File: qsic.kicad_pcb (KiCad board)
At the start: 6 copper layers, 214.1 x 131.7 mm, 217 parts, among them J201 USB_microB, J202 DM3BT-DSF-PEJS, J203 USB_A, J204 DM3BT-DSF-PEJS, J401 QBUS_A, J402 QBUS_B, P201 02x05 Right Angle Shrouded, U101 MT25Q, U102 XC7A75T-1CSG324, U201 FT2232HQ, U202 93LC46C-I/MC, U203 TPS2561, U204 MAX3033E, U205 USB3340, U301 TPS82085, U302 TPS82085, U303 TPS82085, U304 TPS82085, U401 DS8641-LR, U402 DS8641-LR, U403 74LVC8T245, U404 74LVC8T245, U405 74LVC8T245, U406 74LVC8T245, U407 DS8641-LR, U408 DS8641-LR, U409 DS8641-LR, U410 DS8641-LR, U411 74LVC8T245, U412 74LVC8T245, U413 74LVC8T245, U414 74LVC8T245, U415 DS8641-LR, U416 DS8641-LR, U417 74LVC8T245, U418 DS8641-LR, U419 DS8641-LR, U420 74LVC8T245, U421 74LVC8T245, U422 DS8641-LR, U501 MT41J128M16JT-125, U502 TPS51206, X201 ASE-24.000MHz, Y201 12 MHz

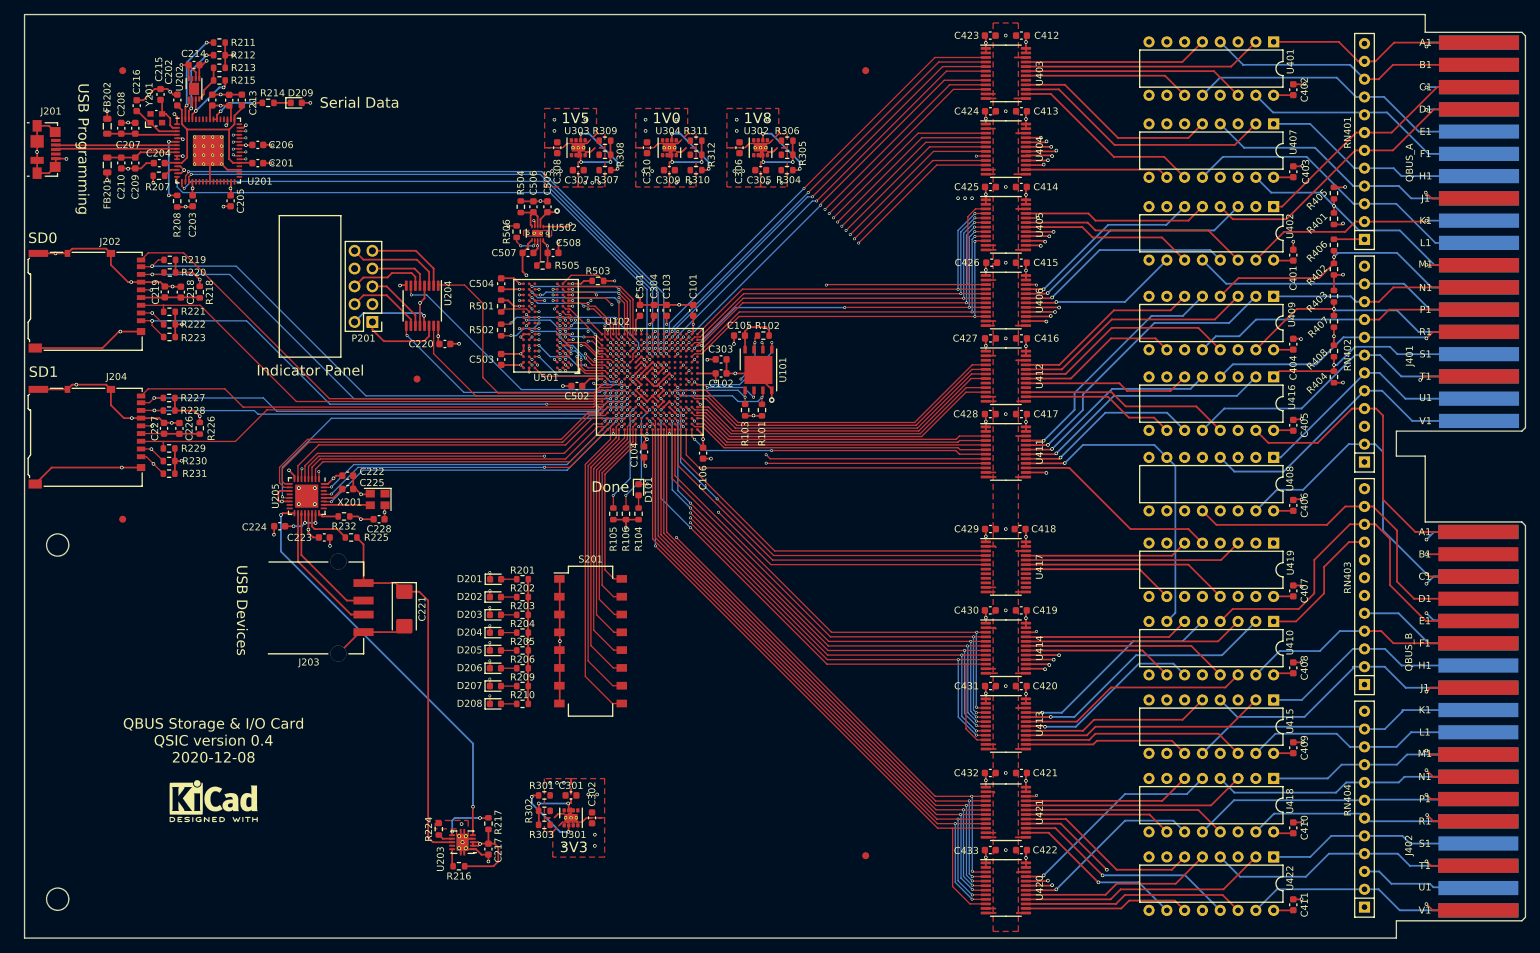
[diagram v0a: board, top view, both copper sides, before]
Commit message: Cleaned up the directory and renamed files.  Also converted from the 324 package on the FPGA to the 484 package.  That conversion is still in-progress.
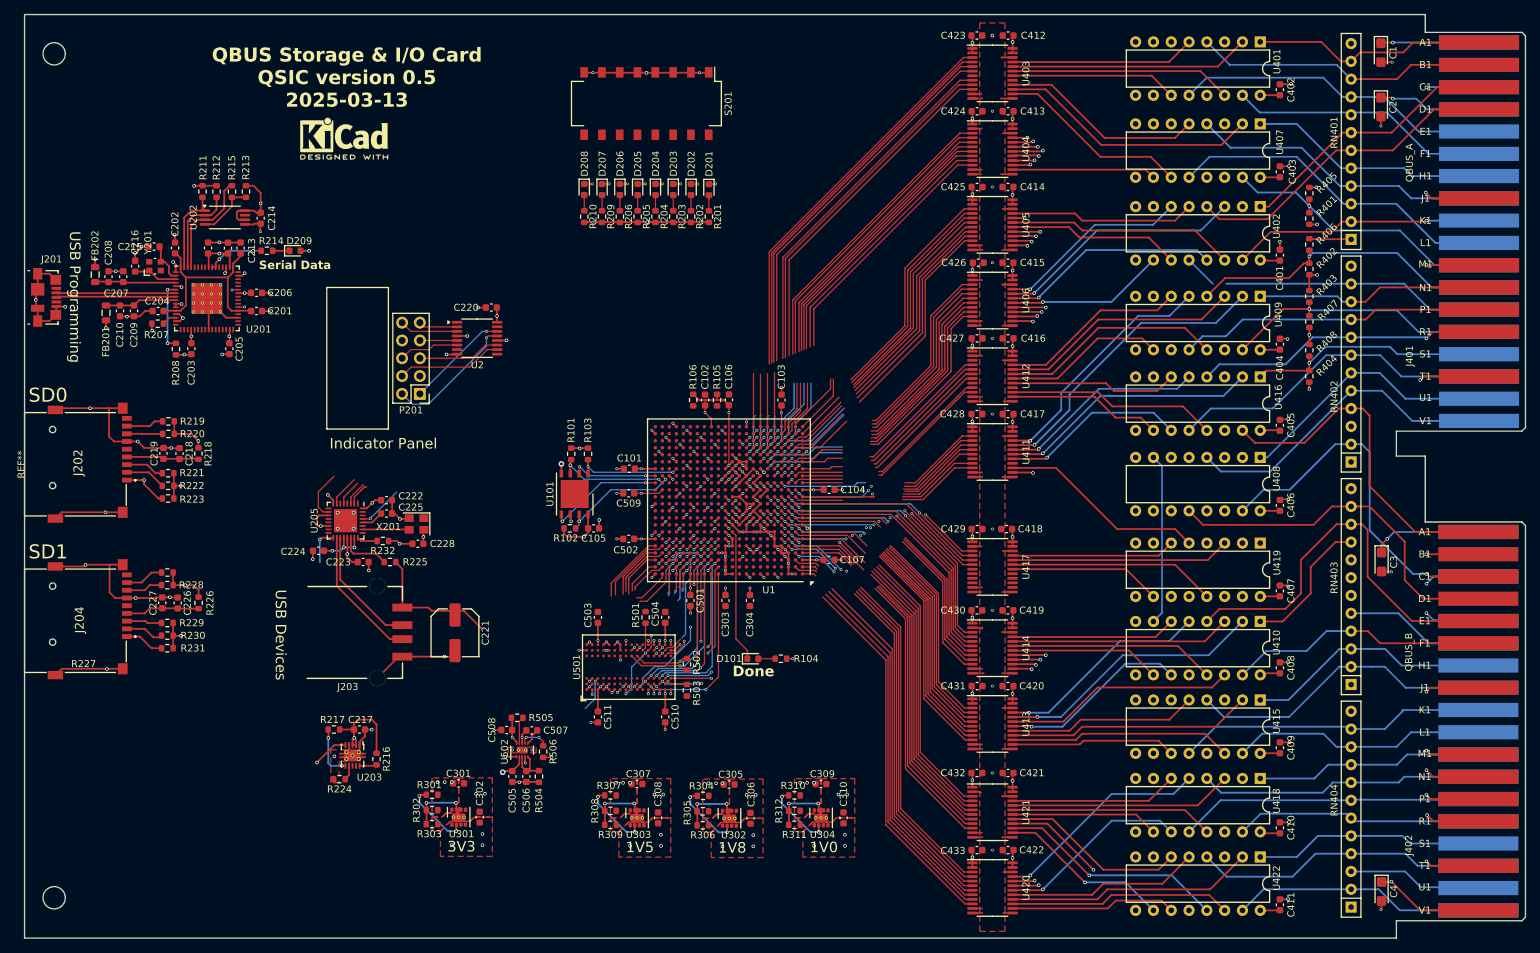
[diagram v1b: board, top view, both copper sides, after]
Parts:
- removed FID101, FID102, FID103, FID104, FID105: Fiducial, Fiducial:Fiducial_1mm_Mask2mm
- removed the REF** at (33.0, 126.3)
- removed U102: XC7A75T-1CSG324, Package_BGA:Xilinx_CSG324
- removed U204: MAX3033E, Package_SO:TSSOP-16_4.4x5mm_P0.65mm
- added C1: 10 uF 16V, Capacitor_Tantalum_SMD:CP_EIA-3216-18_Kemet-A, F.Cu at (226.5, 30.9)
- added C107: 22µF, Capacitor_SMD:C_0603_1608Metric, F.Cu at (147.8, 103.2)
- added C2: 10 uF 16V, Capacitor_Tantalum_SMD:CP_EIA-3216-18_Kemet-A, F.Cu at (226.5, 38.6)
- added C3: 10 uF 16V, Capacitor_Tantalum_SMD:CP_EIA-3216-18_Kemet-A, F.Cu at (226.6, 103.5)
- added C4: 10 uF 16V, Capacitor_Tantalum_SMD:CP_EIA-3216-18_Kemet-A, F.Cu at (226.6, 150.5)
- added C509: 22µF, Capacitor_SMD:C_0603_1608Metric, F.Cu at (119.2, 93.7)
- added C510: 10µF, Capacitor_SMD:C_0603_1608Metric, F.Cu at (124.4, 125.6)
- added C511: 10µF, Capacitor_SMD:C_0603_1608Metric, F.Cu at (114.8, 125.6)
- added REF**: Untitled, DEC:DEChandle QSIC, F.Cu at (33.1, 91.2)
- added U1: XC7A75T-2FGG484, Package_BGA:Xilinx_FGG484, F.Cu at (133.5, 94.7)
- added U2: AM26LV31EIPWR, Package_SO:TSSOP-16_4.4x5mm_P0.65mm, F.Cu at (97.6, 71.6)
- C101, C102, C103, C104, C106, C218, C226, C301, C305, C307, C309, C501, C502: value 22µF 10V -> 22µF
- C221: footprint Capacitor_Tantalum_SMD:CP_EIA-6032-28_Kemet-C -> Capacitor_SMD:C_Elec_6.3x7.7
- C503, C504: value 10µF 10V -> 10µF
- J202, J204: value DM3BT-DSF-PEJS -> TF-15x15; footprint Connector_Card:microSD_HC_Hirose_DM3AT-SF-PEJM5 -> Imports:TF15X15
- R104, R201, R202, R203, R204, R205, R206, R209, R210, R214: value 240 -> 330
- U202: value 93LC46C-I/MC -> 93LC46BT-I/ST; footprint Package_DFN_QFN:DFN-8-1EP_3x2mm_P0.5mm_EP1.75x1.45mm -> Package_SO:TSSOP-8_4.4x3mm_P0.65mm
- moved C310 99.6 mm to (149.9, 140.0), turned to 90 degrees
- moved R312 98.6 mm to (142.9, 141.0), turned to 0 degrees
- moved R306 98.4 mm to (129.8, 141.1), turned to 0 degrees
- moved U304 98.0 mm to (146.7, 140.0), turned to 90 degrees
- moved R309 97.6 mm to (116.6, 141.0), turned to 0 degrees
- moved C308 96.7 mm to (123.4, 140.0), turned to 90 degrees
- moved LOGO101 96.3 mm to (78.6, 43.1)
- moved U303 96.0 mm to (120.4, 140.0), turned to 90 degrees
- moved U302 95.8 mm to (133.6, 140.1), turned to 90 degrees
- moved C306 95.7 mm to (136.6, 140.1), turned to 90 degrees
- moved R311 94.6 mm to (142.9, 139.0), turned to 180 degrees
- moved R305 94.4 mm to (129.8, 139.1), turned to 180 degrees
- moved R308 93.6 mm to (116.6, 139.0), turned to 180 degrees
- moved R310 90.3 mm to (142.9, 136.8), turned to 180 degrees
- moved C309 90.2 mm to (146.6, 135.2), turned to 0 degrees
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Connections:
- net /I/O/D+ renamed /IO/D+
- net /I/O/D- renamed /IO/D-
- P201 pad 1: /I/O/IPdata_P -> /IO/IPdata_P
- P201 pad 10: /I/O/IPclk_N -> /IO/IPclk_N
- P201 pad 2: /I/O/IPdata_N -> /IO/IPdata_N
- P201 pad 4: /I/O/IPlatch_P -> /IO/IPlatch_P
- P201 pad 5: /I/O/IPlatch_N -> /IO/IPlatch_N
- P201 pad 6: /I/O/IPblank_P -> /IO/IPblank_P
- P201 pad 7: /I/O/IPblank_N -> /IO/IPblank_N
- P201 pad 9: /I/O/IPclk_P -> /IO/IPclk_P
- U402 pad 7: /QBUS/~{TxDAL_5} -> GND
- U405 pad 10: /ZDAL19 -> /TDAL19
- U405 pad 3: /ZDAL17 -> /TDAL17
- U405 pad 4: /ZDAL16 -> /TDAL16
- U405 pad 5: /ZWTBT -> /TWTBT
- U405 pad 6: /ZBS7 -> /TBS7
- U405 pad 7: /ZDAL1 -> /TDAL1
- U405 pad 8: /ZDAL0 -> /TDAL0
- U405 pad 9: /ZDAL18 -> /TDAL18
- U406 pad 10: /ZDAL19 -> /RDAL19
- U406 pad 22: /~{RxDAL} -> GND
- U406 pad 3: /ZDAL17 -> /RDAL17
- U406 pad 4: /ZDAL16 -> /RDAL16
- U406 pad 5: /ZWTBT -> /RWTBT
- U406 pad 6: /ZBS7 -> /RBS7
- U406 pad 7: /ZDAL1 -> /RDAL1
- U406 pad 8: /ZDAL0 -> /RDAL0
- U406 pad 9: /ZDAL18 -> /RDAL18
- U408 pad 7: /QBUS/~{TxDAL_5} -> GND
- U410 pad 7: /QBUS/~{TxDAL_5} -> GND
- U411 pad 16: /QBUS/~{TxDAL_5} -> unconnected-(U411-B5-Pad16)
- U411 pad 8: /~{TxDAL} -> unconnected-(U411-A5-Pad8)
- U413 pad 10: /ZDAL6 -> /TDAL6
- U413 pad 3: /ZDAL20 -> /TDAL20
- U413 pad 4: /ZDAL2 -> /TDAL2
- U413 pad 5: /ZDAL21 -> /TDAL21
- U413 pad 6: /ZDAL3 -> /TDAL3
- U413 pad 7: /ZDAL5 -> /TDAL5
- U413 pad 8: /ZDAL4 -> /TDAL4
- U413 pad 9: /ZDAL7 -> /TDAL7
- U414 pad 10: /ZDAL6 -> /RDAL6
- U414 pad 22: /~{RxDAL} -> GND
- U414 pad 3: /ZDAL20 -> /RDAL20
- U414 pad 4: /ZDAL2 -> /RDAL2
- U414 pad 5: /ZDAL21 -> /RDAL21
- U414 pad 6: /ZDAL3 -> /RDAL3
- U414 pad 7: /ZDAL5 -> /RDAL5
- U414 pad 8: /ZDAL4 -> /RDAL4
- U414 pad 9: /ZDAL7 -> /RDAL7
- U415 pad 7: /QBUS/~{TxDAL_5} -> GND
- U418 pad 7: /QBUS/~{TxDAL_5} -> GND
- U420 pad 10: /ZDAL14 -> /TDAL14
- U420 pad 3: /ZDAL9 -> /TDAL9
- U420 pad 4: /ZDAL8 -> /TDAL8
- U420 pad 5: /ZDAL11 -> /TDAL11
- U420 pad 6: /ZDAL10 -> /TDAL10
- U420 pad 7: /ZDAL13 -> /TDAL13
- U420 pad 8: /ZDAL12 -> /TDAL12
- U420 pad 9: /ZDAL15 -> /TDAL15
- U421 pad 10: /ZDAL14 -> /RDAL14
- U421 pad 22: /~{RxDAL} -> GND
- U421 pad 3: /ZDAL9 -> /RDAL9
- U421 pad 4: /ZDAL8 -> /RDAL8
- U421 pad 5: /ZDAL11 -> /RDAL11
- U421 pad 6: /ZDAL10 -> /RDAL10
- U421 pad 7: /ZDAL13 -> /RDAL13
- U421 pad 8: /ZDAL12 -> /RDAL12
- U421 pad 9: /ZDAL15 -> /RDAL15
- U422 pad 7: /QBUS/~{TxDAL_5} -> GND
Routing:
- net /~{RxDAL}: track 132.2 -> 0.00 mm, vias 4 -> 0
- net GND: track 440.5 -> 565.4 mm, vias 148 -> 191
- net /QBUS/~{TxDAL_5}: track 119.8 -> 0.00 mm, vias 1 -> 0
- net /ZDAL14: track 96.6 -> 0.00 mm, vias 2 -> 0
- net /ZDAL12: track 94.6 -> 0.00 mm, vias 2 -> 0
- net /ZDAL15: track 93.7 -> 0.00 mm, vias 2 -> 0
- net /ZDAL10: track 91.8 -> 0.00 mm, vias 2 -> 0
- net /ZDAL13: track 91.8 -> 0.00 mm, vias 2 -> 0
- net /ZDAL9: track 91.3 -> 0.00 mm, vias 4 -> 0
- net /ZDAL8: track 90.0 -> 0.00 mm, vias 2 -> 0
- net /ZDAL11: track 89.9 -> 0.00 mm, vias 2 -> 0
- net /TDO: track 86.0 -> 0.00 mm, vias 2 -> 0
- net /TDI: track 84.5 -> 0.00 mm, vias 2 -> 0
- net /TCK: track 84.4 -> 0.00 mm, vias 2 -> 0
- net /TMS: track 84.3 -> 0.00 mm, vias 2 -> 0
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- removed copper zone on In2.Cu, net /3V3
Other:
- board text added: "QBUS Storage & I/O Card QSIC version ${REVISION} ${ISSUE_DATE}"
- board text removed: "Done"
- board text removed: "QBUS Storage & I/O Card QSIC version 0.4 2020-12-08"

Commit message: Switched the level converters to 74HCT2G04 and 75LVC2G04.  Still need to remap the FPGA pins to the signal odering.
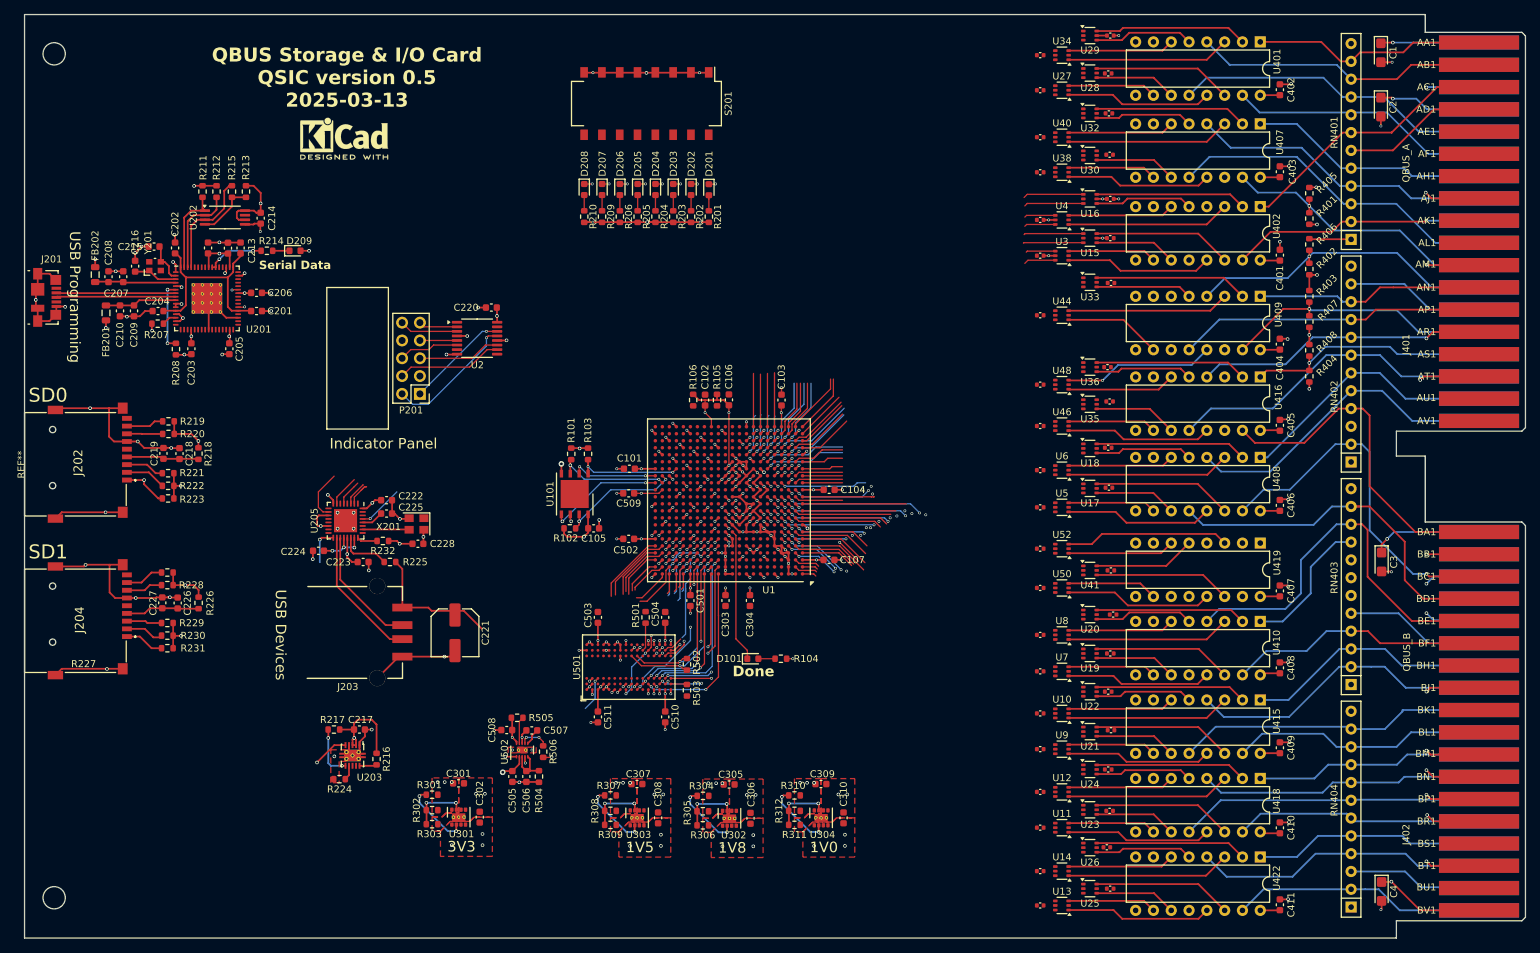
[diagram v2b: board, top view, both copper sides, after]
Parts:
- removed C412, C413, C414, C415, C416, C417, C418, C419, C420, C421, C422, C423, C424, C425, C426, C427, C428, C429, C430, C431, C432, C433: 100nF, Capacitor_SMD:C_0603_1608Metric
- removed U403, U404, U405, U406, U411, U412, U413, U414, U417, U420, U421: 74LVC8T245, Package_SO:TSSOP-24_4.4x7.8mm_P0.65mm
- added C464: 100nF, Capacitor_SMD:C_0402_1005Metric, F.Cu at (177.9, 54.7)
- added C465: 100nF, Capacitor_SMD:C_0402_1005Metric, F.Cu at (177.9, 59.8)
- added C466: 100nF, Capacitor_SMD:C_0402_1005Metric, F.Cu at (177.9, 84.1)
- added C467: 100nF, Capacitor_SMD:C_0402_1005Metric, F.Cu at (177.9, 68.3)
- added C469: 100nF, Capacitor_SMD:C_0402_1005Metric, F.Cu at (177.9, 78.2)
- added C470: 100nF, Capacitor_SMD:C_0402_1005Metric, F.Cu at (177.9, 47.9)
- added C471: 100nF, Capacitor_SMD:C_0402_1005Metric, F.Cu at (177.9, 42.9)
- added C472: 100nF, Capacitor_SMD:C_0402_1005Metric, F.Cu at (177.9, 31.2)
- added C473: 100nF, Capacitor_SMD:C_0402_1005Metric, F.Cu at (177.9, 36.2)
- added C474: 100nF, Capacitor_SMD:C_0402_1005Metric, F.Cu at (177.9, 101.6)
- added C475: 100nF, Capacitor_SMD:C_0402_1005Metric, F.Cu at (177.9, 95.7)
- added C476: 100nF, Capacitor_SMD:C_0402_1005Metric, F.Cu at (177.9, 90.4)
- added C477: 100nF, Capacitor_SMD:C_0402_1005Metric, F.Cu at (187.9, 57.3)
- added C478: 100nF, Capacitor_SMD:C_0402_1005Metric, F.Cu at (187.9, 51.7)
- added C479: 100nF, Capacitor_SMD:C_0402_1005Metric, F.Cu at (187.6, 133.1)
- added C480: 100nF, Capacitor_SMD:C_0402_1005Metric, F.Cu at (187.8, 139.0)
- added C481: 100nF, Capacitor_SMD:C_0402_1005Metric, F.Cu at (187.4, 144.2)
- added C482: 100nF, Capacitor_SMD:C_0402_1005Metric, F.Cu at (187.9, 150.1)
- added C483: 100nF, Capacitor_SMD:C_0402_1005Metric, F.Cu at (187.7, 39.5)
- added C484: 100nF, Capacitor_SMD:C_0402_1005Metric, F.Cu at (187.6, 87.2)
- added C485: 100nF, Capacitor_SMD:C_0402_1005Metric, F.Cu at (187.7, 92.9)
- added C486: 100nF, Capacitor_SMD:C_0402_1005Metric, F.Cu at (188.3, 111.0)
- added C487: 100nF, Capacitor_SMD:C_0402_1005Metric, F.Cu at (187.9, 116.5)
- added C488: 100nF, Capacitor_SMD:C_0402_1005Metric, F.Cu at (187.6, 122.0)
- added C489: 100nF, Capacitor_SMD:C_0402_1005Metric, F.Cu at (188.0, 127.5)
- added C490: 100nF, Capacitor_SMD:C_0402_1005Metric, F.Cu at (177.9, 107.2)
- added C491: 100nF, Capacitor_SMD:C_0402_1005Metric, F.Cu at (187.9, 28.4)
- added C492: 100nF, Capacitor_SMD:C_0402_1005Metric, F.Cu at (177.9, 152.5)
- added C493: 100nF, Capacitor_SMD:C_0402_1005Metric, F.Cu at (187.8, 45.4)
- added C494: 100nF, Capacitor_SMD:C_0402_1005Metric, F.Cu at (177.9, 141.4)
- added C495: 100nF, Capacitor_SMD:C_0402_1005Metric, F.Cu at (188.0, 104.7)
- added C496: 100nF, Capacitor_SMD:C_0402_1005Metric, F.Cu at (177.9, 130.2)
- added C499: 100nF, Capacitor_SMD:C_0402_1005Metric, F.Cu at (187.8, 80.6)
- added C500: 100nF, Capacitor_SMD:C_0402_1005Metric, F.Cu at (177.9, 113.9)
- added C512: 100nF, Capacitor_SMD:C_0402_1005Metric, F.Cu at (187.6, 33.8)
- added C513: 100nF, Capacitor_SMD:C_0402_1005Metric, F.Cu at (177.9, 147.6)
- added C514: 100nF, Capacitor_SMD:C_0402_1005Metric, F.Cu at (188.0, 63.7)
- added C515: 100nF, Capacitor_SMD:C_0402_1005Metric, F.Cu at (177.9, 136.3)
- added C516: 100nF, Capacitor_SMD:C_0402_1005Metric, F.Cu at (187.5, 75.7)
- added C517: 100nF, Capacitor_SMD:C_0402_1005Metric, F.Cu at (177.9, 125.1)
- added C519: 100nF, Capacitor_SMD:C_0402_1005Metric, F.Cu at (177.9, 119.1)
- added U10: 74LVC2GU04, Package_TO_SOT_SMD:SOT-363_SC-70-6, F.Cu at (181.0, 125.1)
- added U11: 74LVC2GU04, Package_TO_SOT_SMD:SOT-363_SC-70-6, F.Cu at (181.0, 141.4)
- added U12: 74LVC2GU04, Package_TO_SOT_SMD:SOT-363_SC-70-6, F.Cu at (181.0, 136.3)
- added U13: 74LVC2GU04, Package_TO_SOT_SMD:SOT-363_SC-70-6, F.Cu at (181.0, 152.5)
- added U14: 74LVC2GU04, Package_TO_SOT_SMD:SOT-363_SC-70-6, F.Cu at (181.0, 147.6)
- added U15: 74HCT2GU04, Package_TO_SOT_SMD:SOT-363_SC-70-6, F.Cu at (185.0, 57.3)
- added U16: 74HCT2GU04, Package_TO_SOT_SMD:SOT-363_SC-70-6, F.Cu at (185.0, 51.7)
- added U17: 74HCT2GU04, Package_TO_SOT_SMD:SOT-363_SC-70-6, F.Cu at (185.0, 93.0)
- added U18: 74HCT2GU04, Package_TO_SOT_SMD:SOT-363_SC-70-6, F.Cu at (185.0, 87.3)
- added U19: 74HCT2GU04, Package_TO_SOT_SMD:SOT-363_SC-70-6, F.Cu at (185.0, 116.5)
- added U20: 74HCT2GU04, Package_TO_SOT_SMD:SOT-363_SC-70-6, F.Cu at (185.0, 111.0)
- added U21: 74HCT2GU04, Package_TO_SOT_SMD:SOT-363_SC-70-6, F.Cu at (185.0, 127.7)
- added U22: 74HCT2GU04, Package_TO_SOT_SMD:SOT-363_SC-70-6, F.Cu at (185.0, 122.0)
- added U23: 74HCT2GU04, Package_TO_SOT_SMD:SOT-363_SC-70-6, F.Cu at (185.0, 138.8)
- added U24: 74HCT2GU04, Package_TO_SOT_SMD:SOT-363_SC-70-6, F.Cu at (185.0, 133.1)
- added U25: 74HCT2GU04, Package_TO_SOT_SMD:SOT-363_SC-70-6, F.Cu at (185.0, 150.1)
- added U26: 74HCT2GU04, Package_TO_SOT_SMD:SOT-363_SC-70-6, F.Cu at (185.0, 144.2)
- added U27: 74LVC2GU04, Package_TO_SOT_SMD:SOT-363_SC-70-6, F.Cu at (181.0, 36.2)
- added U28: 74HCT2GU04, Package_TO_SOT_SMD:SOT-363_SC-70-6, F.Cu at (185.0, 33.8)
- added U29: 74HCT2GU04, Package_TO_SOT_SMD:SOT-363_SC-70-6, F.Cu at (185.0, 28.4)
- added U3: 74LVC2GU04, Package_TO_SOT_SMD:SOT-363_SC-70-6, F.Cu at (181.0, 59.8)
- added U30: 74HCT2GU04, Package_TO_SOT_SMD:SOT-363_SC-70-6, F.Cu at (185.0, 45.5)
- added U32: 74HCT2GU04, Package_TO_SOT_SMD:SOT-363_SC-70-6, F.Cu at (185.0, 39.5)
- added U33: 74HCT2GU04, Package_TO_SOT_SMD:SOT-363_SC-70-6, F.Cu at (185.0, 63.6)
- added U34: 74LVC2GU04, Package_TO_SOT_SMD:SOT-363_SC-70-6, F.Cu at (181.0, 31.2)
- added U35: 74HCT2GU04, Package_TO_SOT_SMD:SOT-363_SC-70-6, F.Cu at (185.0, 81.0)
- added U36: 74HCT2GU04, Package_TO_SOT_SMD:SOT-363_SC-70-6, F.Cu at (185.0, 75.7)
- added U38: 74LVC2GU04, Package_TO_SOT_SMD:SOT-363_SC-70-6, F.Cu at (181.0, 47.9)
- added U4: 74LVC2GU04, Package_TO_SOT_SMD:SOT-363_SC-70-6, F.Cu at (181.0, 54.7)
- added U40: 74LVC2GU04, Package_TO_SOT_SMD:SOT-363_SC-70-6, F.Cu at (181.0, 42.9)
- added U41: 74HCT2GU04, Package_TO_SOT_SMD:SOT-363_SC-70-6, F.Cu at (185.0, 104.7)
- added U44: 74LVC2GU04, Package_TO_SOT_SMD:SOT-363_SC-70-6, F.Cu at (181.0, 68.3)
- added U46: 74LVC2GU04, Package_TO_SOT_SMD:SOT-363_SC-70-6, F.Cu at (181.0, 84.1)
- added U48: 74LVC2GU04, Package_TO_SOT_SMD:SOT-363_SC-70-6, F.Cu at (181.0, 78.2)
- added U5: 74LVC2GU04, Package_TO_SOT_SMD:SOT-363_SC-70-6, F.Cu at (181.0, 95.7)
- added U50: 74LVC2GU04, Package_TO_SOT_SMD:SOT-363_SC-70-6, F.Cu at (181.0, 107.2)
- added U52: 74LVC2GU04, Package_TO_SOT_SMD:SOT-363_SC-70-6, F.Cu at (181.0, 101.6)
- added U6: 74LVC2GU04, Package_TO_SOT_SMD:SOT-363_SC-70-6, F.Cu at (181.0, 90.4)
- added U7: 74LVC2GU04, Package_TO_SOT_SMD:SOT-363_SC-70-6, F.Cu at (181.0, 119.1)
- added U8: 74LVC2GU04, Package_TO_SOT_SMD:SOT-363_SC-70-6, F.Cu at (181.0, 113.9)
- added U9: 74LVC2GU04, Package_TO_SOT_SMD:SOT-363_SC-70-6, F.Cu at (181.0, 130.2)
- J401, J402: footprint DEC:DEC_Edge_Fingers_single_height -> myMods:DEC_Edge_Fingers_single_height-1
- moved J402 0.10 mm to (234.4, 98.2)
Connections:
- U409 pad 6: Net-(U409-out4) -> unconnected-(U409-out4-Pad6)
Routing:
- net GND: track 565.4 -> 398.7 mm, vias 191 -> 182
- net /TIRQ6: track 65.7 -> 9.22 mm
- net /TIRQ5: track 63.2 -> 7.60 mm
- net /TRPLY: track 64.2 -> 9.28 mm
- net /TDOUT: track 61.6 -> 7.70 mm
- net /TDAL14: track 55.3 -> 2.02 mm
- net /TDAL15: track 56.1 -> 3.29 mm
- net /TDAL12: track 54.6 -> 2.22 mm
- net /TDAL13: track 55.6 -> 3.67 mm
- net /TSYNC: track 60.1 -> 8.15 mm
- net /TDIN: track 61.4 -> 10.4 mm
- net /TIRQ4: track 58.0 -> 8.11 mm
- net /TDAL10: track 55.9 -> 6.62 mm
- net /TDAL11: track 56.9 -> 8.03 mm
- net /TDAL8: track 57.7 -> 9.32 mm
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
